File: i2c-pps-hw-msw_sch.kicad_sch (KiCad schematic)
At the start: 0 parts

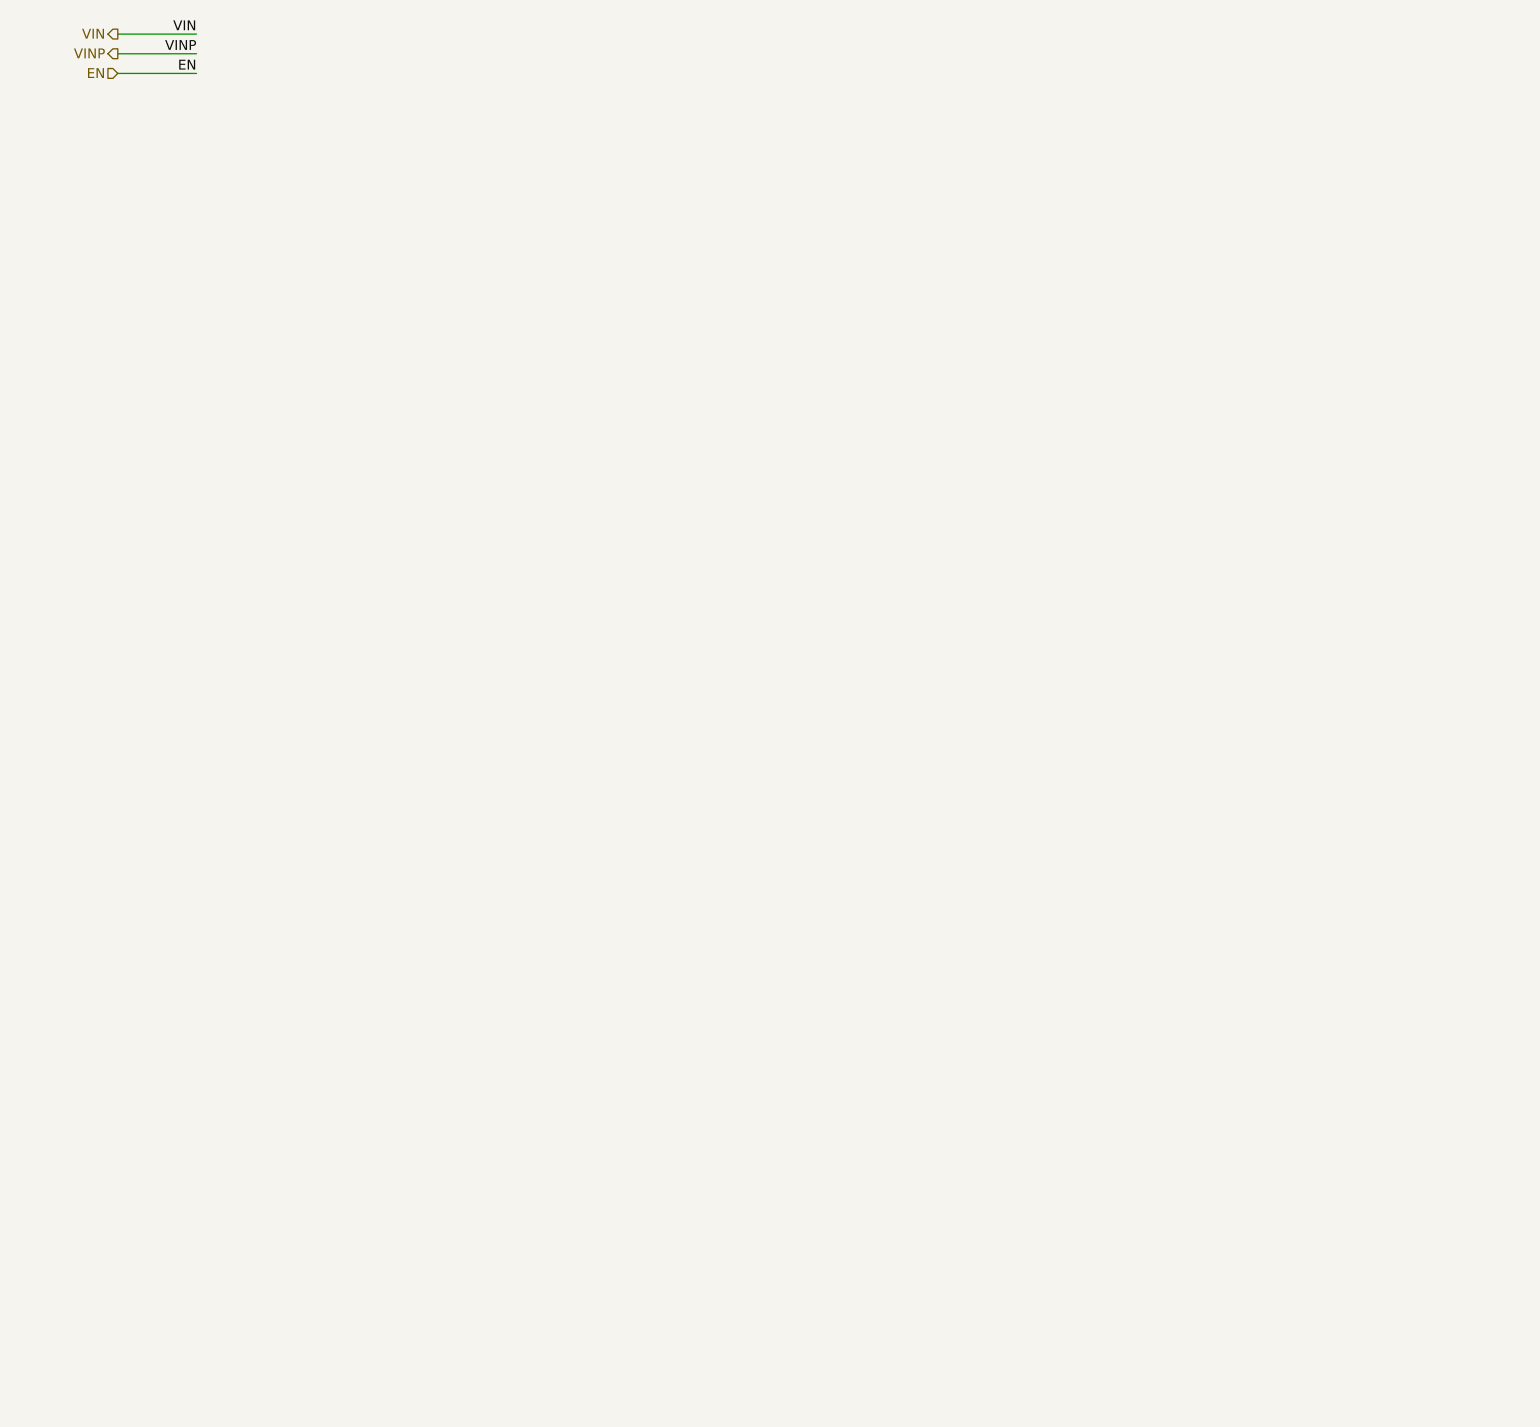
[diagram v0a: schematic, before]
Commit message: Design schematics and set per component requirements
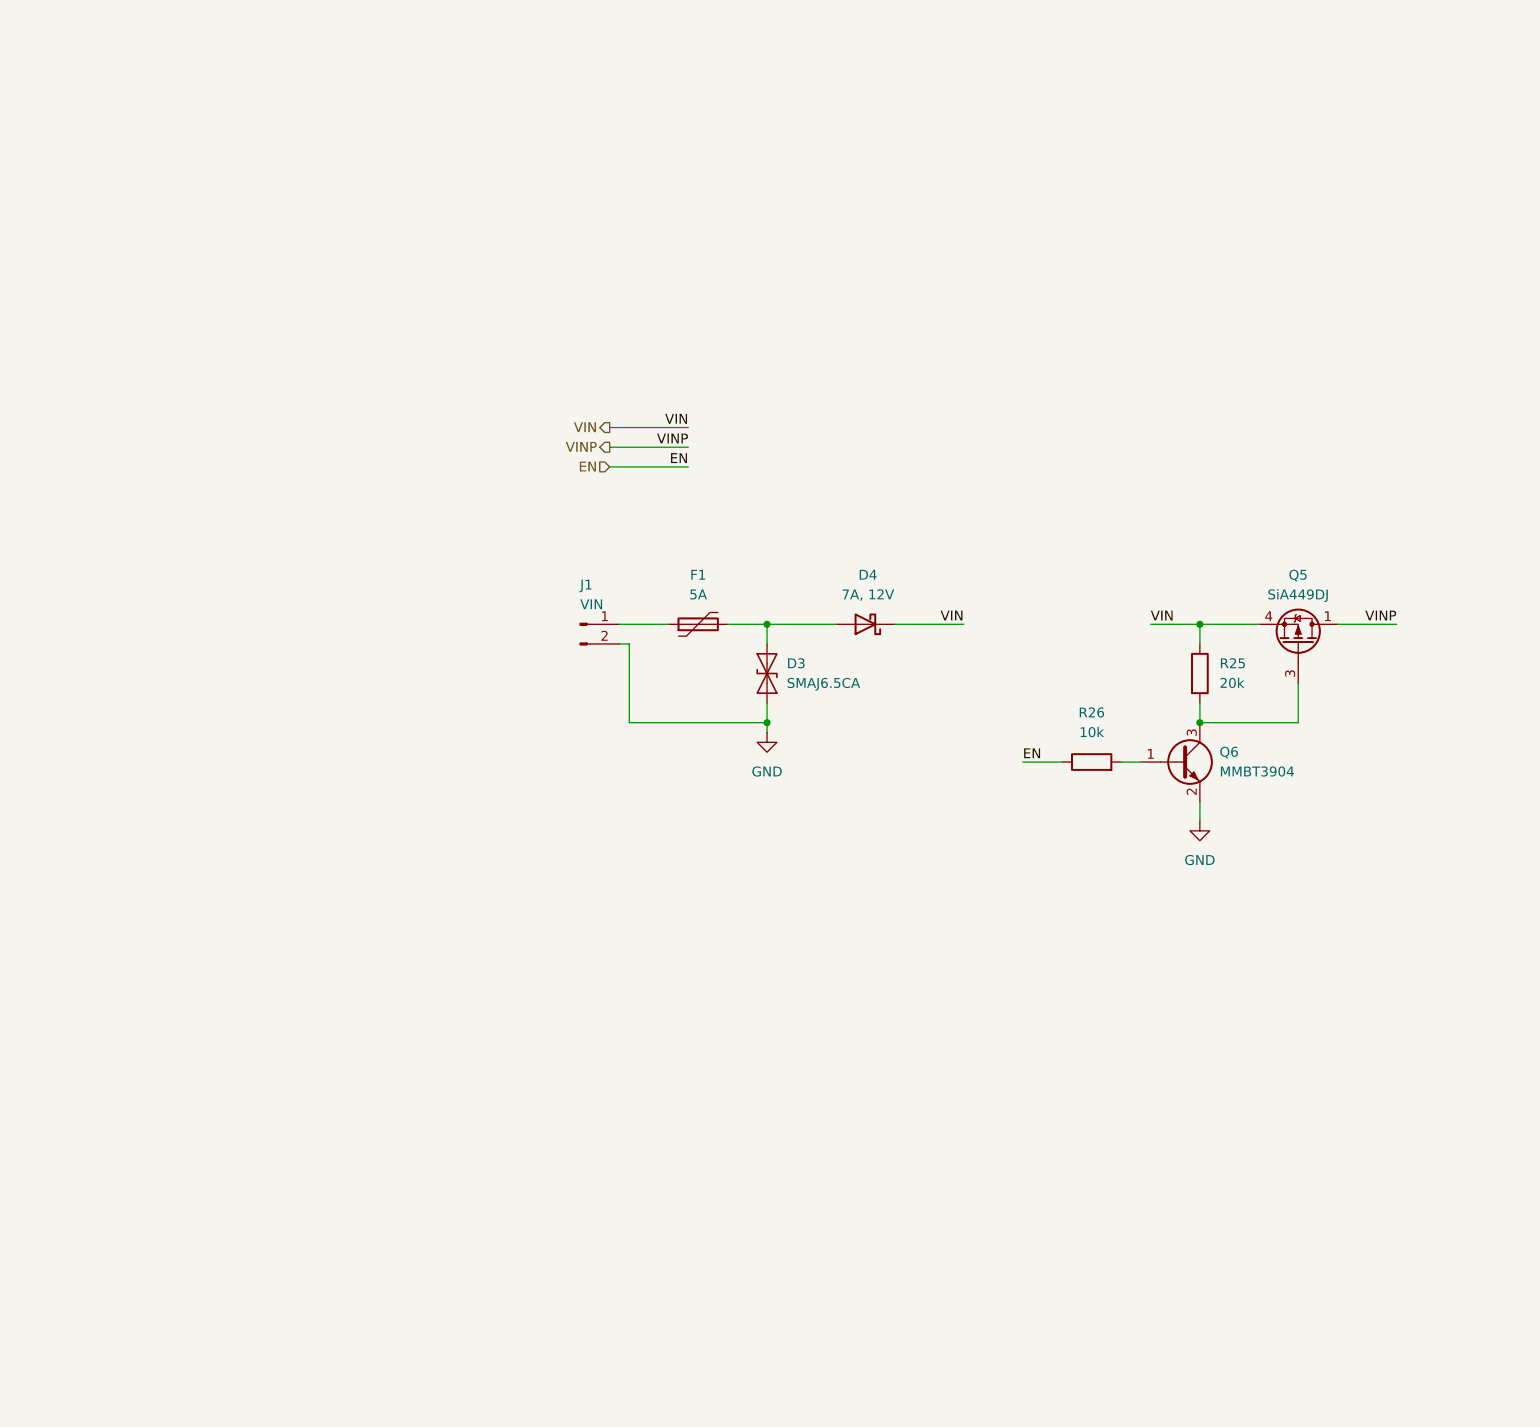
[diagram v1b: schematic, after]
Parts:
- added D3: SMAJ6.5CA, Diode_SMD:D_SMA, symbol Diode:SMAJ6.5CA
- added D4: 7A, 12V, symbol Device:D_Schottky
- added F1: 5A, symbol Device:Polyfuse
- added J1: VIN, symbol Connector:Conn_01x02_Pin
- added Q5: SiA449DJ, Package_TO_SOT_SMD:Vishay_PowerPAK_SC70-6L_Single, symbol Transistor_FET:SiA449DJ
- added Q6: MMBT3904, Package_TO_SOT_SMD:SOT-23, symbol Transistor_BJT:MMBT3904
- added R25: 20k, Resistor_SMD:R_0603_1608Metric_Pad0.98x0.95mm_HandSolder, symbol Device:R
- added R26: 10k, Resistor_SMD:R_0603_1608Metric_Pad0.98x0.95mm_HandSolder, symbol Device:R
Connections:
- net EN: now also R26.1
- net VIN: now also D4.1 (K), Q5.4 (S), R25.1
- net VINP: now also Q5.1 (D)
- new net: F1.1, J1.1 (Pin_1)
- new net: D3.2 (A2), D4.2 (A), F1.2
- new net: Q6.1 (B), R26.2
- new net: Q5.3 (G), Q6.3 (C), R25.2
- new net GND: D3.1 (A1), J1.2 (Pin_2), Q6.2 (E)

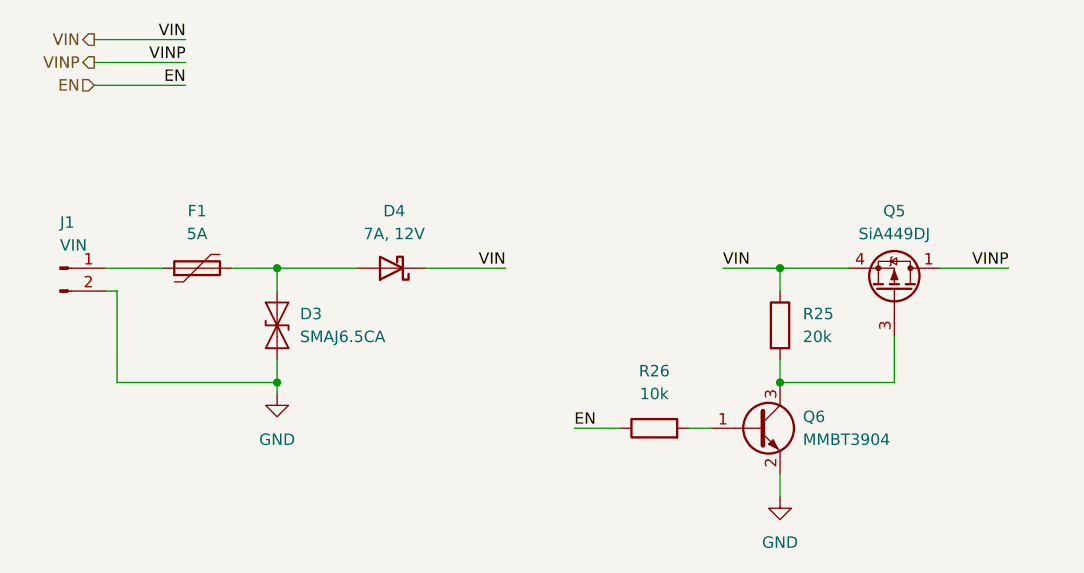
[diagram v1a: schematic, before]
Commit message: Rename VIN to +5V_Prot for clarity
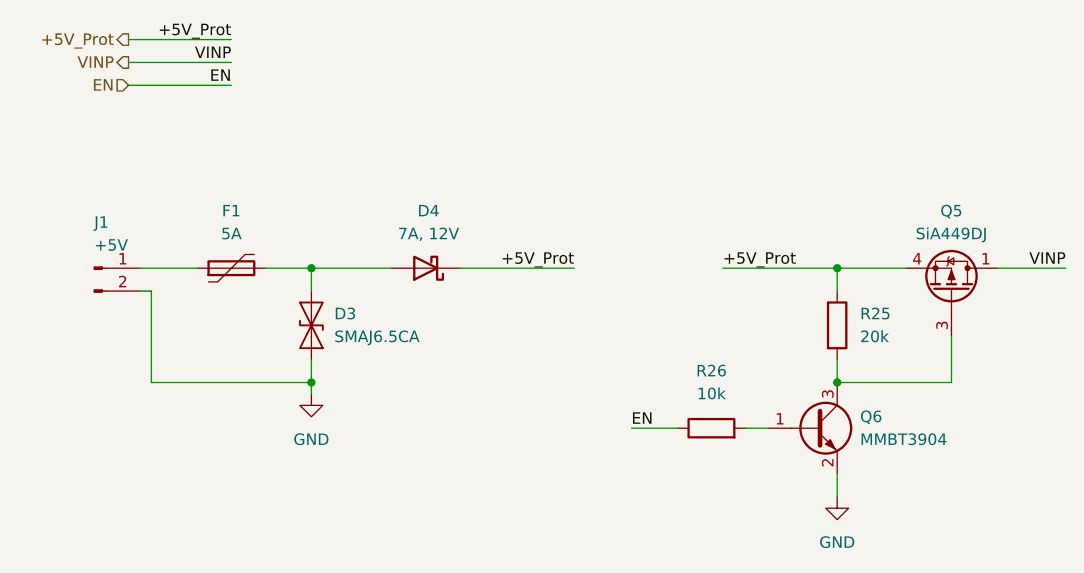
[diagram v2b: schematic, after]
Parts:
- J1: value VIN -> +5V
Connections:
- net VIN renamed +5V_Prot
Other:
- moved on the sheet: D3, D4, F1, J1, Q5, Q6, R25, R26

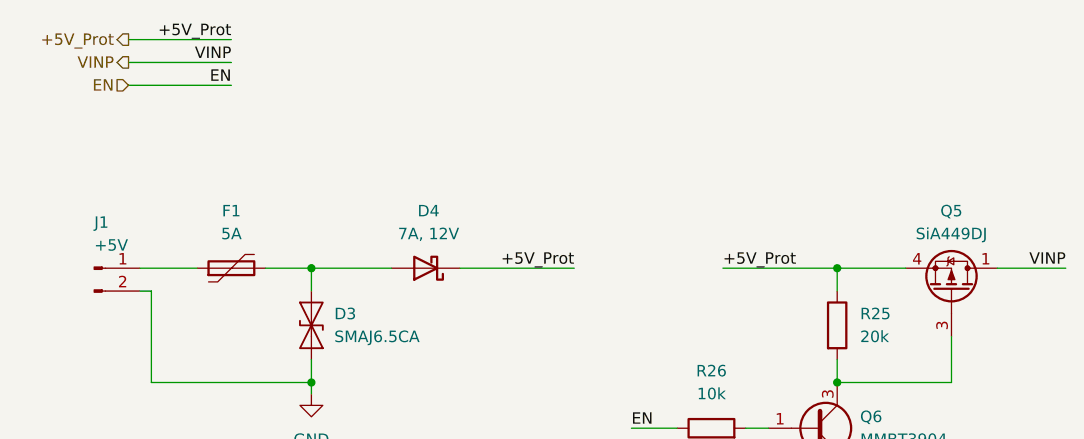
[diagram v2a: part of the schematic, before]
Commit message: Rename VINP to +5V_Run for clarity
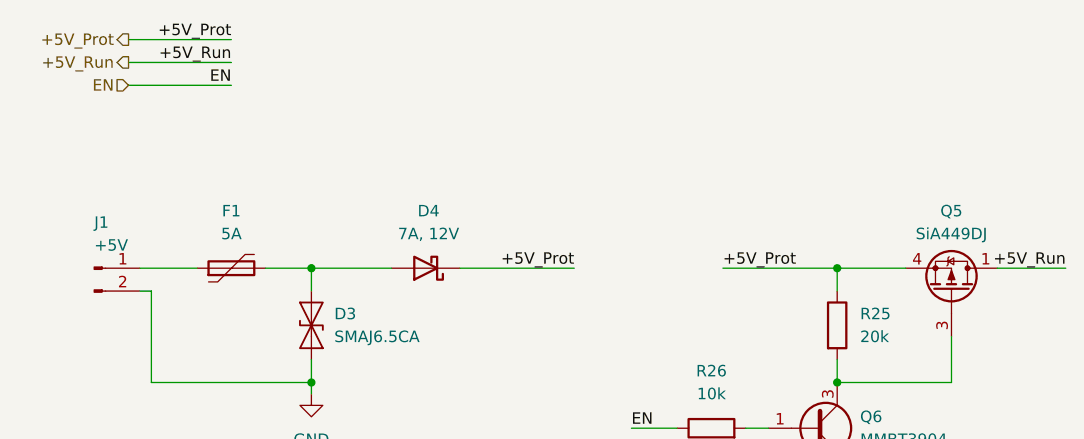
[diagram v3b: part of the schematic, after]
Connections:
- net VINP renamed +5V_Run
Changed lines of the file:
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@@
 		)
 	)
-	(label "VINP"
+	(label "+5V_Run"
 		(at 196.85 101.6 180)
 		(effects
@@
 		)
 	)
-	(label "VINP"
+	(label "+5V_Run"
 		(at 104.14 78.74 180)
 		(effects
@@
 		)
 	)
-	(hierarchical_label "VINP"
+	(hierarchical_label "+5V_Run"
 		(shape output)
 		(at 92.71 78.74 180)

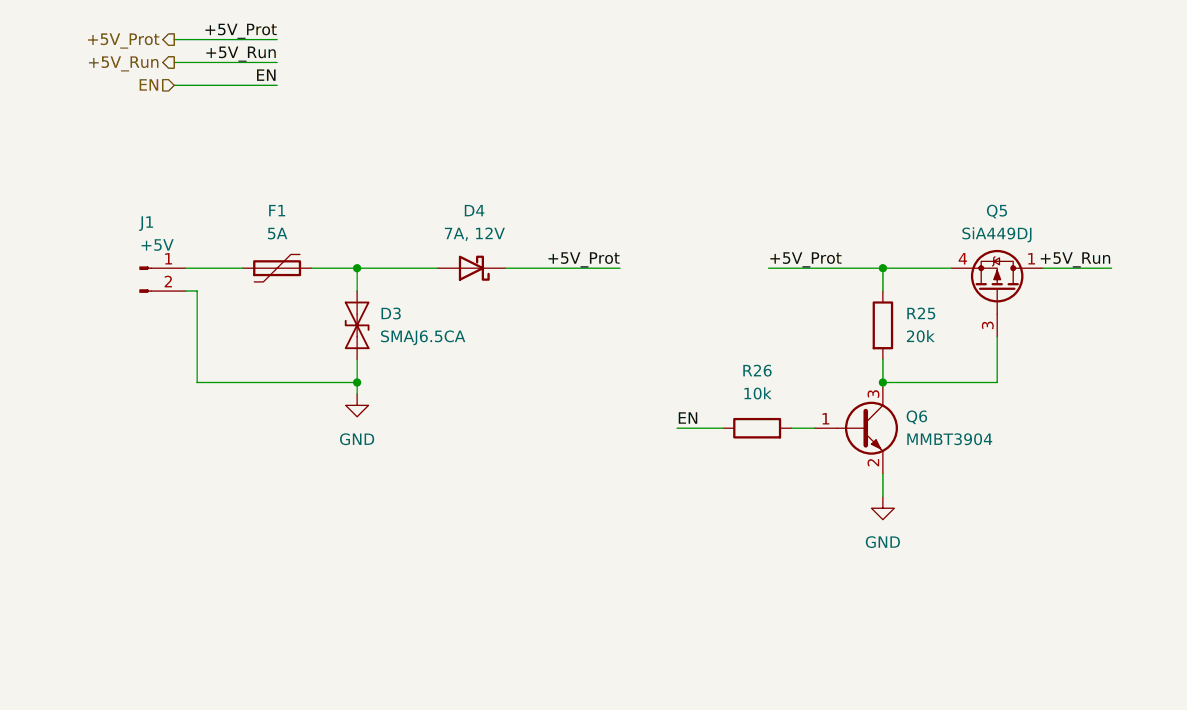
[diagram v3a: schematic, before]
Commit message: Add more indicator LEDs
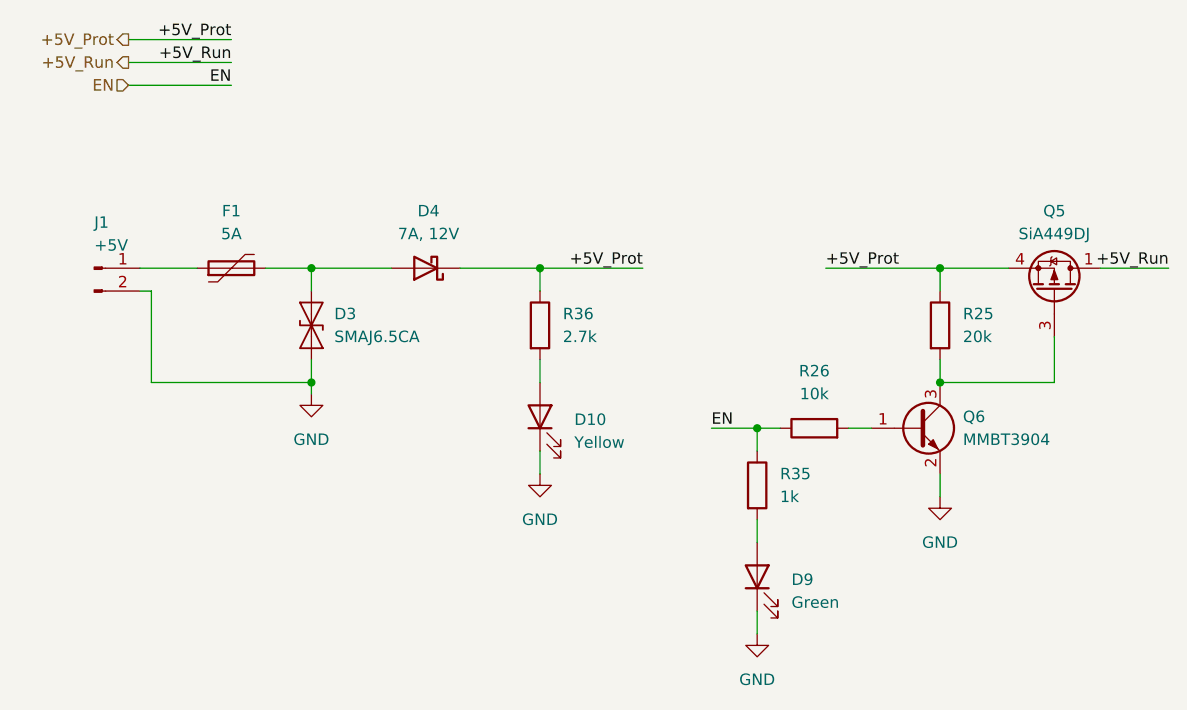
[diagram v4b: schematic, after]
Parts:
- added D10: Yellow, LED_SMD:LED_0603_1608Metric_Pad1.05x0.95mm_HandSolder, symbol Device:LED
- added D9: Green, LED_SMD:LED_0603_1608Metric_Pad1.05x0.95mm_HandSolder, symbol Device:LED
- added R35: 1k, Resistor_SMD:R_0603_1608Metric_Pad0.98x0.95mm_HandSolder, symbol Device:R
- added R36: 2.7k, Resistor_SMD:R_0603_1608Metric_Pad0.98x0.95mm_HandSolder, symbol Device:R
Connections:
- net +5V_Prot: now also R36.1
- net EN: now also R35.1
- net GND: now also D10.1 (K), D9.1 (K)
- new net: D10.2 (A), R36.2
- new net: D9.2 (A), R35.2
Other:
- moved on the sheet: D3, D4, F1, J1, Q5, Q6, R25, R26
